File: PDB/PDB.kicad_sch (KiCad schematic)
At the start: 27 parts

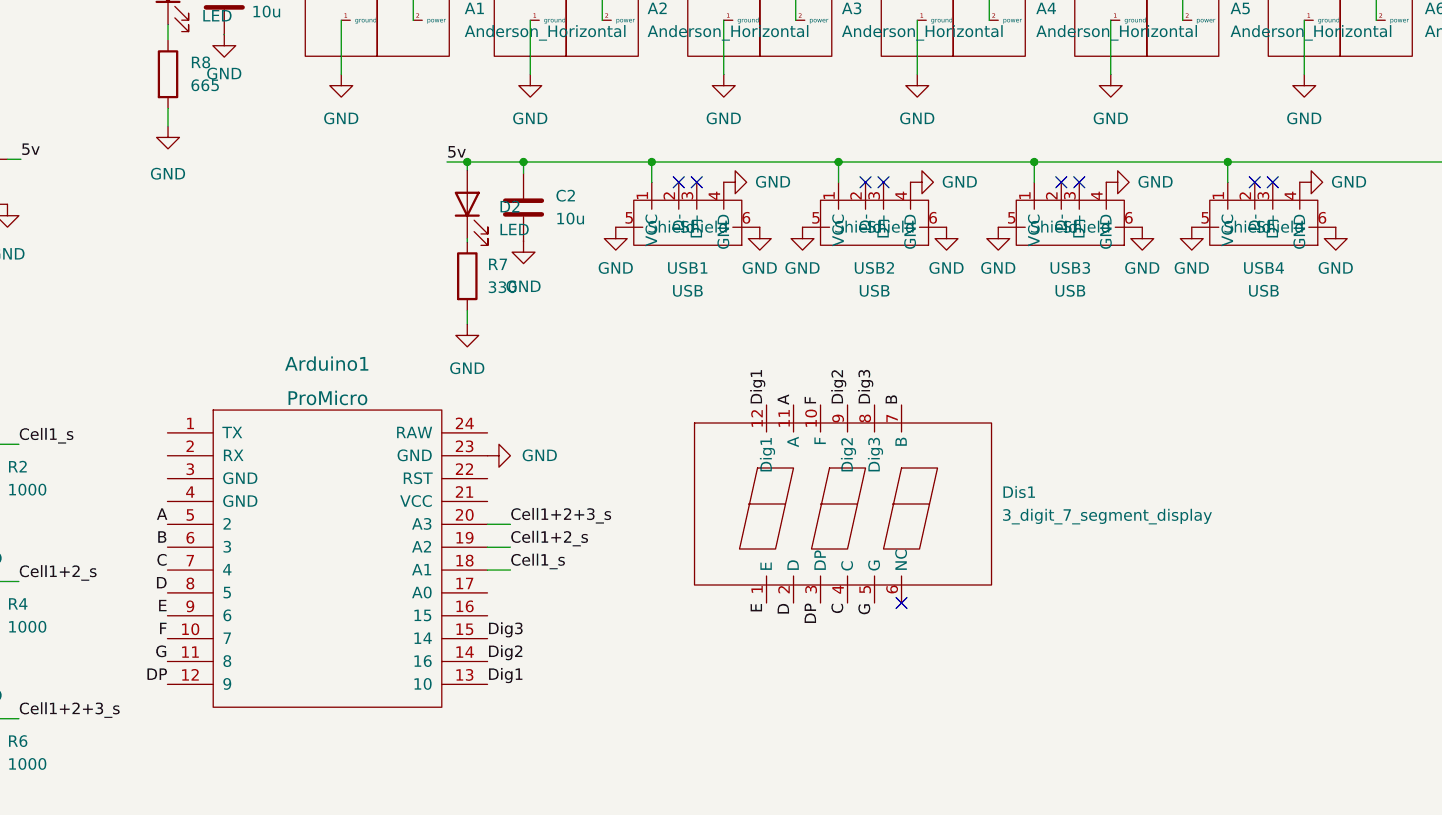
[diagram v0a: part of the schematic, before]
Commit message: Finished 7Seg display
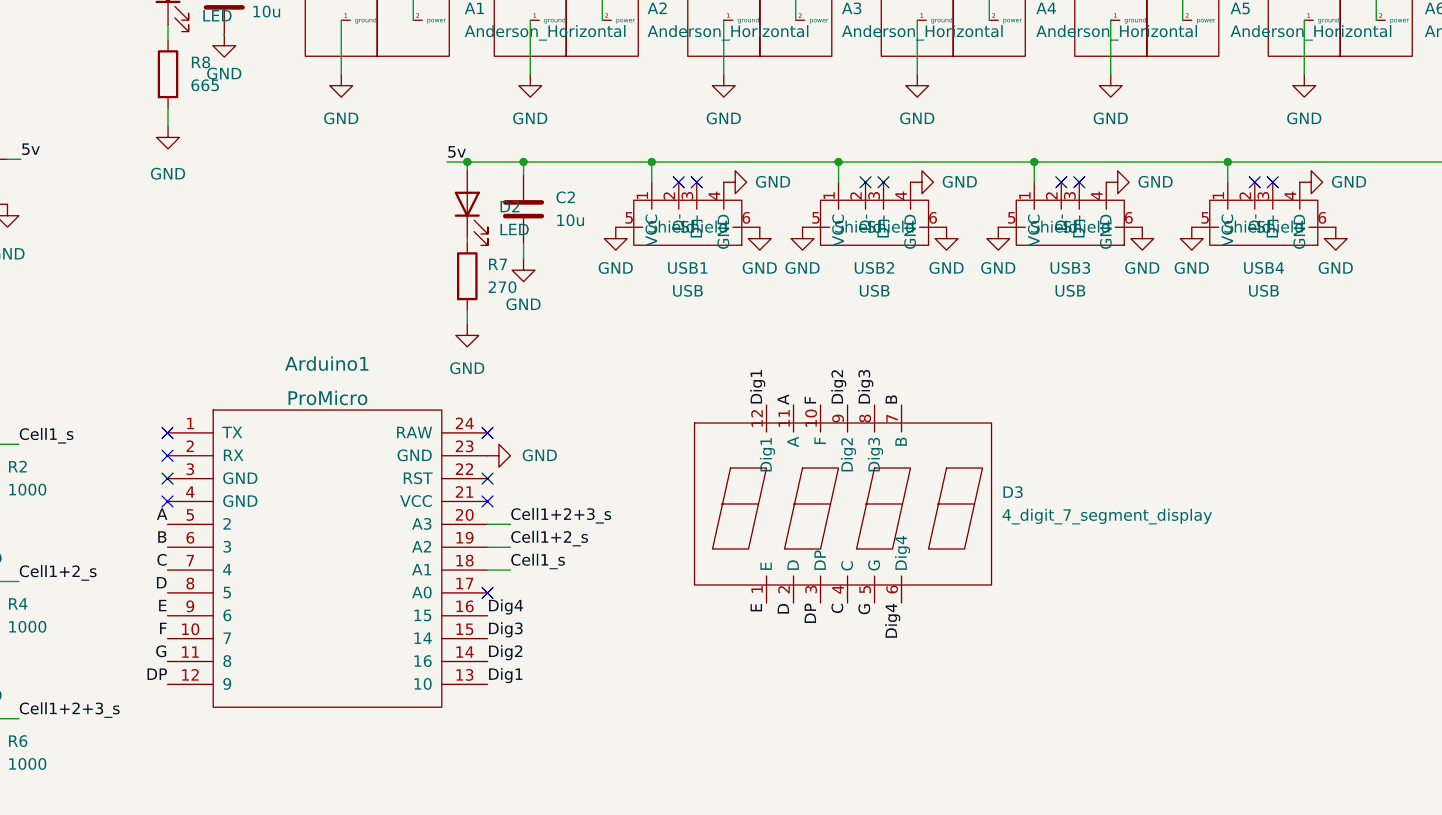
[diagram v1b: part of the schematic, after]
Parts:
- removed Dis1: 3_digit_7_segment_display, symbol PiE_Symbols:3_digit_7_segment_display
- added D3: 4_digit_7_segment_display, symbol PiE_Symbols:4_digit_7_segment_display
- R7: value 330 -> 270
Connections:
- net A: now also D3.11 (A)
- net B: now also D3.7 (B)
- net C: now also D3.4 (C)
- net D: now also D3.2 (D)
- net DP: now also D3.3 (DP)
- net Dig1: now also D3.12 (Dig1)
- net Dig2: now also D3.9 (Dig2)
- net Dig3: now also D3.8 (Dig3)
- net E: now also D3.1 (E)
- net F: now also D3.10 (F)
- net G: now also D3.5 (G)
- net GND: now also C2.2
- net Dig4: now reaches Arduino1.16 (15)
- net Dig4: now also D3.6 (Dig4)
- no-connect marks 9 -> 16

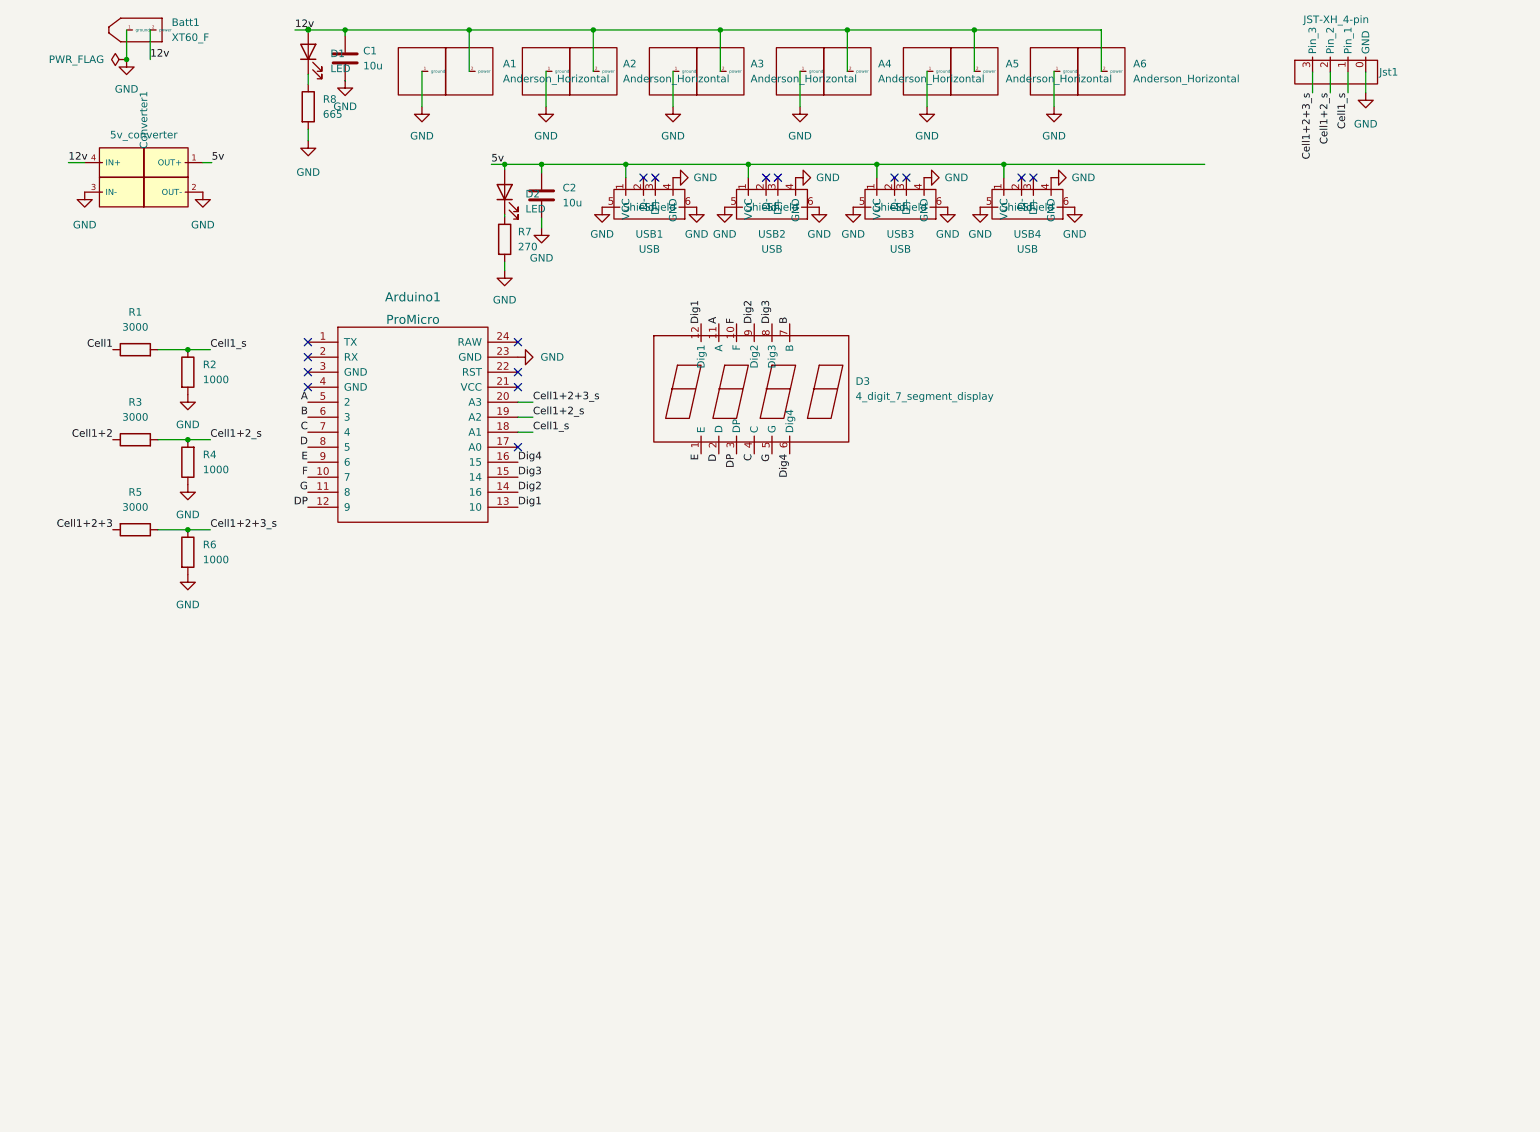
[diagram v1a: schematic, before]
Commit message: added resistors to common anode
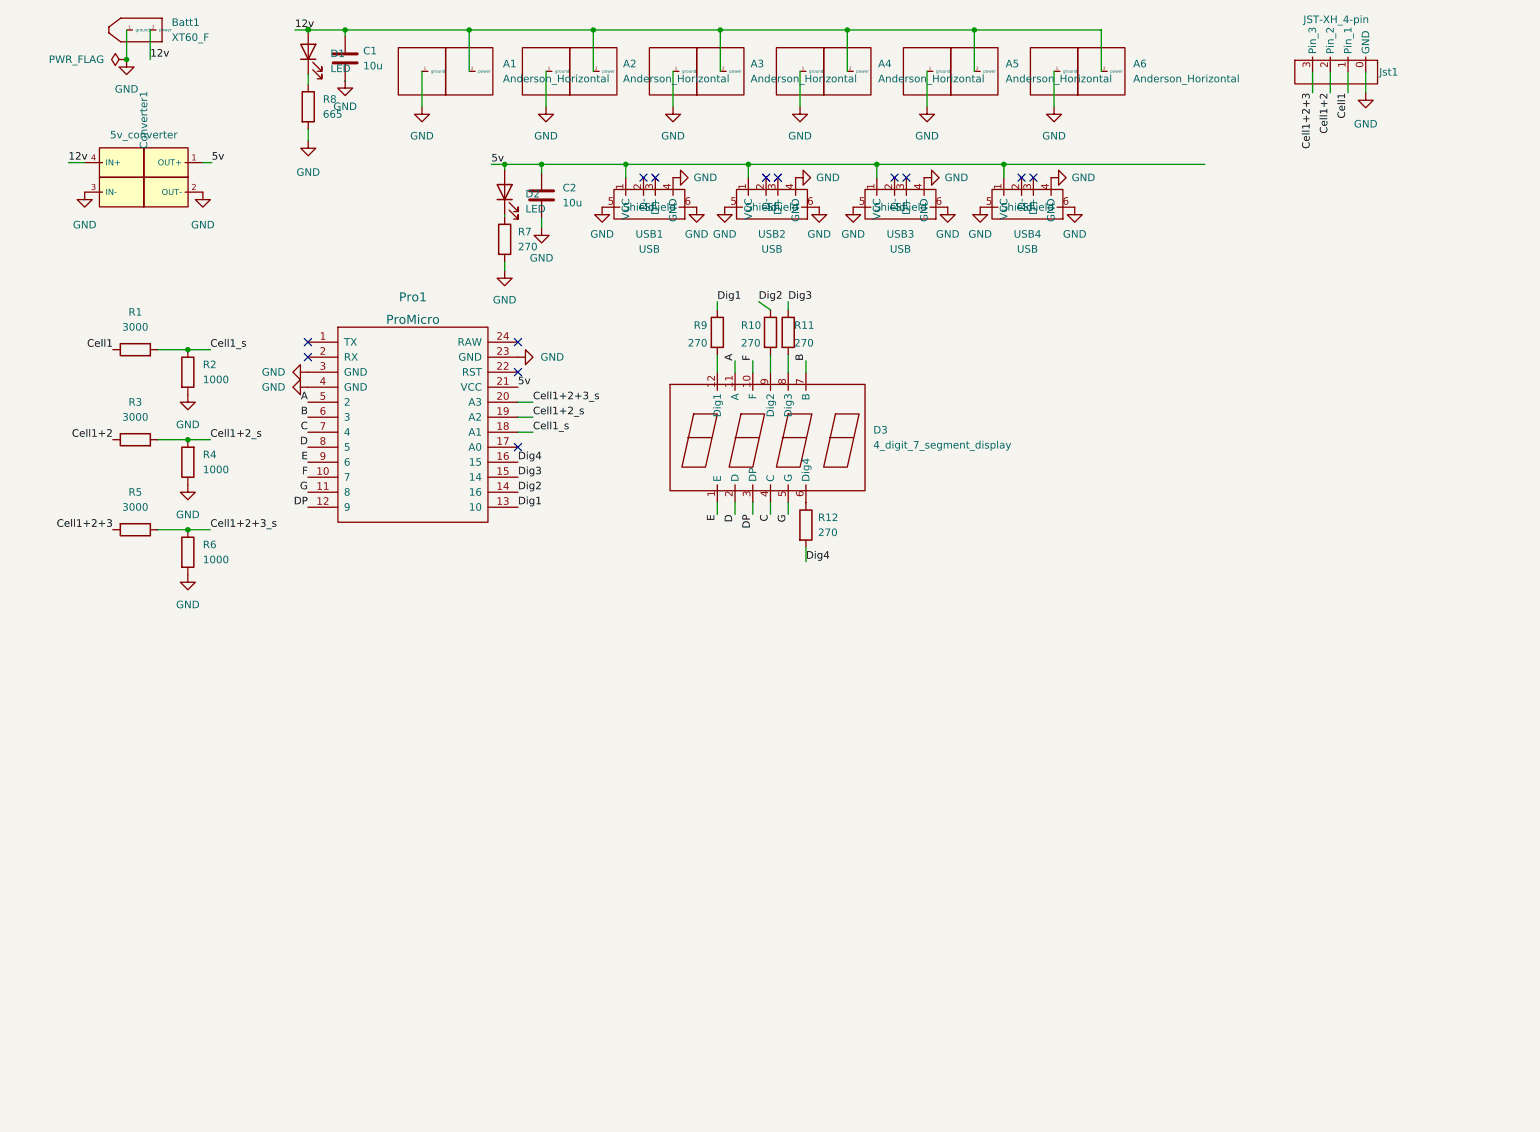
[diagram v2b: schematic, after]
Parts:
- removed Arduino1: ProMicro, symbol PiE_Symbols:ProMicro
- added Pro1: ProMicro, symbol PiE_Symbols:ProMicro
- added R10, R11, R12, R9: 270, symbol Device:R
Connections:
- net 5v: now also Pro1.21 (VCC)
- net A: now also Pro1.5 (2)
- net B: now also Pro1.6 (3)
- net C: now also Pro1.7 (4)
- net Cell1: now also Jst1.1 (Pin_1)
- net Cell1+2: now also Jst1.2 (Pin_2)
- net Cell1+2+3: now also Jst1.3 (Pin_3)
- net Cell1+2+3_s: now also Pro1.20 (A3); no longer Jst1.3 (Pin_3)
- net Cell1+2_s: now also Pro1.19 (A2); no longer Jst1.2 (Pin_2)
- net Cell1_s: now also Pro1.18 (A1); no longer Jst1.1 (Pin_1)
- net D: now also Pro1.8 (5)
- net DP: now also Pro1.12 (9)
- net Dig1: now also Pro1.13 (10), R9.1; no longer D3.12 (Dig1)
- net Dig2: now also Pro1.14 (16), R10.1; no longer D3.9 (Dig2)
- net Dig3: now also Pro1.15 (14), R11.1; no longer D3.8 (Dig3)
- net Dig4: now also Pro1.16 (15), R12.2; no longer D3.6 (Dig4)
- net E: now also Pro1.9 (6)
- net F: now also Pro1.10 (7)
- net G: now also Pro1.11 (8)
- net GND: now also Pro1.23 (GND), Pro1.3 (GND), Pro1.4 (GND)
- new net: D3.12 (Dig1), R9.2
- new net: D3.6 (Dig4), R12.1
- new net: D3.8 (Dig3), R11.2
- new net: D3.9 (Dig2), R10.2
- no-connect marks 16 -> 13
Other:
- moved on the sheet: D3

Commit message: don't remember what this update is?
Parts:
- added B1: Buzzer, symbol PiE_Symbols:Buzzer
- added R13: R, symbol Device:R
- R10, R11, R12, R9: value 270 -> 150
- R7: value 270 -> 470
- R8: value 665 -> 1.1k
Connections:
- net 12v: no longer Batt1.2 (power)
- net GND: now also R13.1
- net Buzzer: now reaches Pro1.17 (A0)
- net Buzzer: now also B1.1 (input)
- new net: B1.2 (output), R13.2
- new net switch in: Batt1.2 (power)
- no-connect marks 13 -> 12
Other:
- note added: "A0 = Digital pin 18"
- moved on the sheet: Converter1

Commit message: finished Schematic
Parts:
- added F1: Fuseholder, symbol PiE_Symbols:Fuseholder
- added Sw1: D-SWITCH_MR5-111-C5N-BB, symbol PiE_Symbols:D-SWITCH_MR5-111-C5N-BB
- R10, R11, R12, R9: value 150 -> 120
- R13: value R -> 100
- R7: value 470 -> 200
- R8: value 1.1k -> 680
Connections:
- net 12v: now also F1.3 (out1), F1.4 (out2)
- net switch in: now also Sw1.1 (In)
- new net switch out: F1.1 (in1), F1.2 (in2), Sw1.2 (Out)
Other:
- moved on the sheet: B1, C2, Converter1, D2, D3, Jst1, Pro1, R1, R10, R11, R12, R13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

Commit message: gonna actually do some work
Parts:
- added Q?: S8050, Package_TO_SOT_THT:TO-92_Inline, symbol Transistor_BJT:S8050
- added R14: 1000, symbol Device:R_Small
- R1, R3, R5: value 3000 -> 30000; footprint (none) -> Resistor_SMD:R_0805_2012Metric
- R13: value 100 -> 3300
- R2, R4, R6: value 1000 -> 10000; footprint (none) -> Resistor_SMD:R_0805_2012Metric
- R7: value 200 -> 120
- R8: value 680 -> 590
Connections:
- net 5v: now also B1.1 (input), R14.1
- net Buzzer: now also R13.1; no longer B1.1 (input)
- net GND: now also Q?.1 (E); no longer R13.1
- net at B1.2 (output): now also Q?.3 (C), R14.2; no longer R13.2
- new net: Q?.2 (B), R13.2
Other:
- moved on the sheet: B1

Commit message: Fixed seg dis and added buzzer amp circuit
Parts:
- added JP1: Jumper_2_Open, symbol Jumper:Jumper_2_Open
- added R13, R14, R7, R8: 200, symbol Device:R
- R10, R11, R12, R9: value 120 -> 200
- gave numbers to parts that had none: 1
- renumbered R13 to R15, R14 to R16, R8 to R17, R7 to R18
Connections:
- net A: now also Pro1.11 (8), R12.1; no longer D3.11 (A), Pro1.5 (2)
- net B: now also Pro1.12 (9), R14.1; no longer D3.7 (B), Pro1.6 (3)
- net Buzzer: now also Pro1.13 (10); no longer Pro1.17 (A0)
- net C: now also Pro1.10 (7), R10.2; no longer D3.4 (C), Pro1.7 (4)
- net D: now also Pro1.5 (2), R8.2; no longer D3.2 (D), Pro1.8 (5)
- net DP: now also Pro1.1 (TX), R9.2; no longer D3.3 (DP), Pro1.12 (9)
- net Dig1: now also D3.12 (Dig1), Pro1.9 (6); no longer Pro1.13 (10), R9.1
- net Dig2: now also D3.9 (Dig2), Pro1.8 (5); no longer Pro1.14 (16), R10.1
- net Dig3: now also D3.8 (Dig3), Pro1.7 (4); no longer Pro1.15 (14), R11.1
- net Dig4: now also D3.6 (Dig4), Pro1.6 (3); no longer Pro1.16 (15), R12.2
- net E: now also Pro1.2 (RX), R7.2; no longer D3.1 (E), Pro1.9 (6)
- net F: now also Pro1.15 (14), R13.1; no longer D3.10 (F), Pro1.10 (7)
- net G: now also Pro1.14 (16), R11.2; no longer D3.5 (G), Pro1.11 (8)
- net GND: now also JP1.2 (B)
- net at Q1.2 (B), R15.2: now also JP1.1 (A)
- new net: D3.1 (E), R7.1
- new net: D3.10 (F), R13.2
- new net: D3.11 (A), R12.2
- new net: D3.2 (D), R8.1
- new net: D3.3 (DP), R9.1
- new net: D3.4 (C), R10.1
- new net: D3.5 (G), R11.1
- new net: D3.7 (B), R14.2
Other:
- moved on the sheet: B1, D3, Pro1, R15, R16

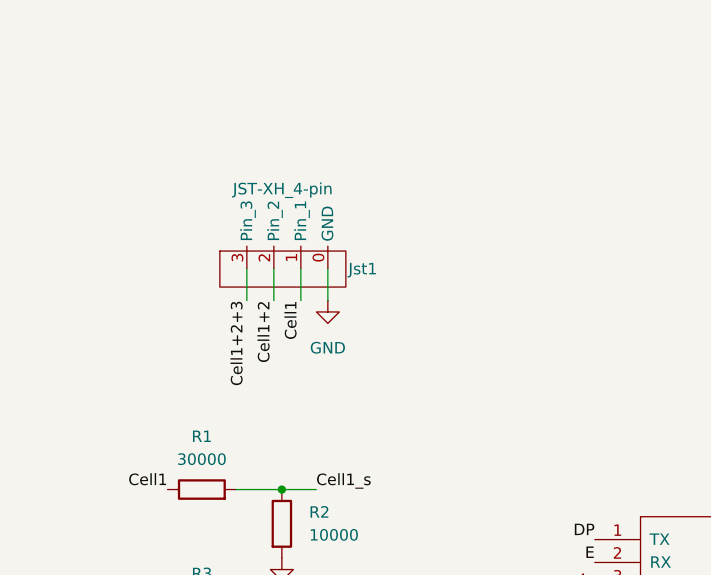
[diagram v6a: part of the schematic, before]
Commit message: Started footprints
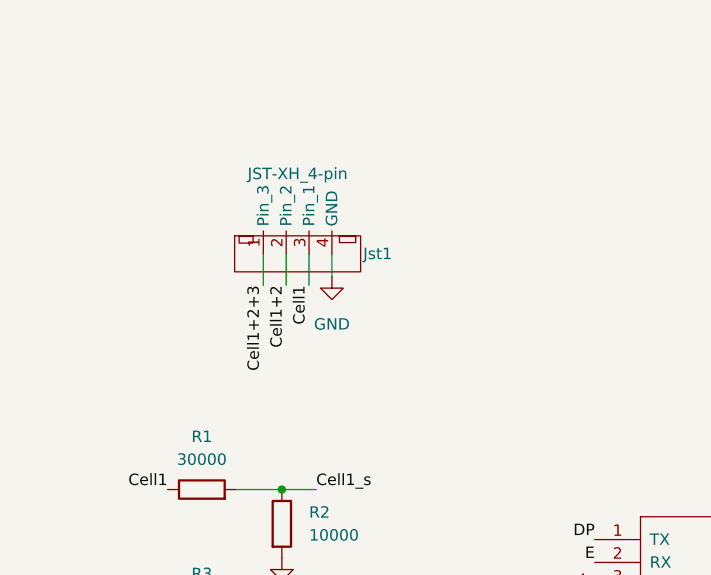
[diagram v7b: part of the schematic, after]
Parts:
- B1: footprint (none) -> PiE_Footprints:Buzzer
- D1, D2: footprint (none) -> LED_SMD:LED_0201_0603Metric
- D3: footprint (none) -> PiE_Footprints:LED-SEG-TH_12P-L30.0-W13.7-P2.54-S10.16-BL
- F1: footprint (none) -> PiE_Footprints:Fuse Holder SMD
- JP1: footprint (none) -> Connector_PinHeader_2.54mm:PinHeader_1x02_P2.54mm_Vertical
- Jst1: footprint (none) -> PiE_Footprints:JST_XH_B4B-XH-AM_1x04_P2.50mm_Vertical
- Pro1: footprint (none) -> PiE_Footprints:ProMicro-EnforcedTop
- R1, R2, R3, R4, R5, R6: footprint Resistor_SMD:R_0805_2012Metric -> Resistor_SMD:R_0603_1608Metric
- R10, R11, R12, R13, R14, R15, R16, R18, R7, R8, R9: footprint (none) -> Resistor_SMD:R_0603_1608Metric
- R17: footprint (none) -> Resistor_SMD:R_1210_3225Metric
- Sw1: footprint (none) -> PiE_Footprints:Rocker Switch
- USB1, USB2, USB3, USB4: footprint (none) -> PiE_Footprints:USB-A_female
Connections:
- net Cell1: now also Jst1.3 (Pin_1); no longer Jst1.1 (Pin_1)
- net Cell1+2+3: now also Jst1.1 (Pin_3); no longer Jst1.3 (Pin_3)
- net GND: now also Jst1.4 (GND); no longer Jst1.0 (GND)
